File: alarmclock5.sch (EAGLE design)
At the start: 39 parts, among them X1 MKDSN1,5/2-5,08, X2 MKDSN1,5/2-5,08, X3 MKDSN1,5/2-5,08, X4 MKDSN1,5/2-5,08

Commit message: new schema
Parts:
- added C16: 330uF/25V, SparkFun-Passives:CAP_POLPTH2
- added Q1: FDN360P, transistor-power:FDN360P
- added R11: 10k, SparkFun-Passives:RESISTOR0603-RES
- added T1: 2N2222, transistor:2N2222
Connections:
- new net N$40: T1.B, U$5.IO8
- new net N$41: Q1.G, R11.1, T1.C
- new net N$43: Q1.S, R11.2, U$1.VCC, U$2.VIN+
- net GND: now also C16.-, T1.E
- net VCC: now also C16.+, Q1.D; no longer U$1.VCC, U$2.VIN+
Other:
- moved on the sheet: C11, U$1, U$2, U$4
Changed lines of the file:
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@@
 <part name="U$1" library="mouser" deviceset="163-179PH-EX" device=""/>
 <part name="U$2" library="mouser" deviceset="709-SMU02N-05" device=""/>
-<part name="SUPPLY1" library="SparkFun-Aesthetics" deviceset="VCC" device=""/>
 <part name="GND1" library="SparkFun-Aesthetics" deviceset="GND" device=""/>
 <part name="U$4" library="mouser" deviceset="USB_TYPEA_CONNECTOR" device=""/>
@@
 <part name="C15" library="SparkFun-Capacitors" deviceset="CAP" device="0603-CAP" value="2200pF50V"/>
 <part name="SUPPLY30" library="supply2" deviceset="GND" device=""/>
+<part name="T1" library="transistor" deviceset="2N2222" device=""/>
+<part name="GND2" library="SparkFun-Aesthetics" deviceset="GND" device=""/>
+<part name="R11" library="SparkFun-Passives" deviceset="RESISTOR" device="0603-RES" value="10k"/>
+<part name="Q1" library="transistor-power" deviceset="FDN360P" device=""/>
+<part name="GND3" library="SparkFun-Aesthetics" deviceset="GND" device=""/>
+<part name="SUPPLY31" library="SparkFun-Aesthetics" deviceset="VCC" device=""/>
+<part name="C16" library="SparkFun-Passives" deviceset="CAP_POL" device="PTH2" value="330uF/25V"/>
 </parts>
 <sheets>
 <sheet>
 <plain>
-<text x="152.4" y="76.2" size="1.778" layer="91">18V</text>
+<text x="-83.82" y="-132.08" size="1.778" layer="91">18V</text>
 </plain>
 <instances>
-<instance part="U$1" gate="G$1" x="139.7" y="76.2"/>
-<instance part="U$2" gate="G$1" x="96.52" y="73.66"/>
-<instance part="SUPPLY1" gate="G$1" x="127" y="78.74"/>
-<instance part="GND1" gate="1" x="127" y="71.12"/>
-<instance part="U$4" gate="G$1" x="45.72" y="76.2"/>
+<instance part="U$1" gate="G$1" x="-96.52" y="-132.08"/>
+<instance part="U$2" gate="G$1" x="-139.7" y="-134.62"/>
+<instance part="GND1" gate="1" x="-109.22" y="-137.16"/>
+<instance part="U$4" gate="G$1" x="-190.5" y="-132.08"/>
 <instance part="U$3" gate="G$1" x="116.84" y="-17.78"/>
 <instance part="GND4" gate="1" x="157.48" y="-63.5"/>
@@
 <instance part="R3" gate="G$1" x="129.54" y="-78.74" rot="R90"/>
 <instance part="R1" gate="G$1" x="114.3" y="-15.24" rot="R90"/>
-<instance part="C11" gate="G$1" x="73.66" y="76.2"/>
+<instance part="C11" gate="G$1" x="-162.56" y="-132.08"/>
 <instance part="SUPPLY6" gate="GND" x="127" y="-7.62" rot="R180"/>
 <instance part="+3V1" gate="G$1" x="-20.32" y="27.94"/>
@@
 <instance part="C15" gate="G$1" x="101.6" y="-48.26" rot="R90"/>
 <instance part="SUPPLY30" gate="GND" x="106.68" y="-48.26" rot="R90"/>
+<instance part="T1" gate="G$1" x="-50.8" y="-96.52" rot="MR0"/>
+<instance part="GND2" gate="1" x="-53.34" y="-106.68" rot="MR0"/>
+<instance part="R11" gate="G$1" x="-53.34" y="-81.28" rot="MR90"/>
+<instance part="Q1" gate="G$1" x="-66.04" y="-93.98" rot="MR0"/>
+<instance part="GND3" gate="1" x="-78.74" y="-109.22" rot="MR0"/>
+<instance part="SUPPLY31" gate="G$1" x="-78.74" y="-99.06" rot="MR0"/>
+<instance part="C16" gate="G$1" x="-78.74" y="-101.6" rot="MR0"/>
 </instances>
 <busses>
@@
 <segment>
 <pinref part="U$2" gate="G$1" pin="VO+"/>
-<wire x1="63.5" y1="78.74" x2="73.66" y2="78.74" width="0.1524" layer="91"/>
+<wire x1="-172.72" y1="-129.54" x2="-162.56" y2="-129.54" width="0.1524" layer="91"/>
 <pinref part="U$4" gate="G$1" pin="VCC"/>
-<wire x1="73.66" y1="78.74" x2="86.36" y2="78.74" width="0.1524" layer="91"/>
-<wire x1="35.56" y1="83.82" x2="35.56" y2="91.44" width="0.1524" layer="91"/>
-<wire x1="35.56" y1="91.44" x2="63.5" y2="91.44" width="0.1524" layer="91"/>
-<wire x1="63.5" y1="91.44" x2="63.5" y2="78.74" width="0.1524" layer="91"/>
+<wire x1="-162.56" y1="-129.54" x2="-149.86" y2="-129.54" width="0.1524" layer="91"/>
+<wire x1="-200.66" y1="-124.46" x2="-200.66" y2="-116.84" width="0.1524" layer="91"/>
+<wire x1="-200.66" y1="-116.84" x2="-172.72" y2="-116.84" width="0.1524" layer="91"/>
+<wire x1="-172.72" y1="-116.84" x2="-172.72" y2="-129.54" width="0.1524" layer="91"/>
 <pinref part="C11" gate="G$1" pin="+"/>
-<junction x="73.66" y="78.74"/>
+<junction x="-162.56" y="-129.54"/>
 </segment>
 </net>
 <net name="VCC" class="1">
-<segment>
-<pinref part="U$2" gate="G$1" pin="VIN+"/>
-<pinref part="U$1" gate="G$1" pin="VCC"/>
-<wire x1="111.76" y1="78.74" x2="127" y2="78.74" width="0.1524" layer="91"/>
-<pinref part="SUPPLY1" gate="G$1" pin="VCC"/>
-<wire x1="127" y1="78.74" x2="134.62" y2="78.74" width="0.1524" layer="91"/>
-<junction x="127" y="78.74"/>
-</segment>
 <segment>
 <pinref part="SUPPLY5" gate="G$1" pin="VCC"/>
@@
 <junction x="157.48" y="-50.8"/>
 </segment>
+<segment>
+<pinref part="SUPPLY31" gate="G$1" pin="VCC"/>
+<pinref part="C16" gate="G$1" pin="+"/>
+<pinref part="Q1" gate="G$1" pin="D"/>
+<wire x1="-68.58" y1="-99.06" x2="-78.74" y2="-99.06" width="0.1524" layer="91"/>
+</segment>
 </net>
 <net name="GND" class="1">
@@
 <pinref part="U$1" gate="G$1" pin="GND"/>
 <pinref part="U$2" gate="G$1" pin="VIN-"/>
-<wire x1="134.62" y1="73.66" x2="127" y2="73.66" width="0.1524" layer="91"/>
+<wire x1="-101.6" y1="-134.62" x2="-109.22" y2="-134.62" width="0.1524" layer="91"/>
 <pinref part="GND1" gate="1" pin="GND"/>
-<wire x1="127" y1="73.66" x2="111.76" y2="73.66" width="0.1524" layer="91"/>
-<junction x="127" y="73.66"/>
-<wire x1="134.62" y1="73.66" x2="134.62" y2="68.58" width="0.1524" layer="91"/>
-<wire x1="134.62" y1="68.58" x2="154.94" y2="68.58" width="0.1524" layer="91"/>
+<wire x1="-109.22" y1="-134.62" x2="-124.46" y2="-134.62" width="0.1524" layer="91"/>
+<junction x="-109.22" y="-134.62"/>
+<wire x1="-101.6" y1="-134.62" x2="-101.6" y2="-139.7" width="0.1524" layer="91"/>
+<wire x1="-101.6" y1="-139.7" x2="-81.28" y2="-139.7" width="0.1524" layer="91"/>
 <pinref part="U$1" gate="G$1" pin="GND1"/>
-<wire x1="154.94" y1="68.58" x2="154.94" y2="76.2" width="0.1524" layer="91"/>
-<junction x="134.62" y="73.66"/>
+<wire x1="-81.28" y1="-139.7" x2="-81.28" y2="-132.08" width="0.1524" layer="91"/>
+<junction x="-101.6" y="-134.62"/>
 </segment>
 <segment>
@@
 <pinref part="C15" gate="G$1" pin="2"/>
 <pinref part="SUPPLY30" gate="GND" pin="GND"/>
+</segment>
+<segment>
+<pinref part="T1" gate="G$1" pin="E"/>
+<pinref part="GND2" gate="1" pin="GND"/>
+<wire x1="-53.34" y1="-104.14" x2="-53.34" y2="-101.6" width="0.1524" layer="91"/>
+</segment>
+<segment>
+<pinref part="C16" gate="G$1" pin="-"/>
+<pinref part="GND3" gate="1" pin="GND"/>
 </segment>
 </net>
@@
 <segment>
 <pinref part="U$2" gate="G$1" pin="VO-"/>
-<wire x1="86.36" y1="73.66" x2="76.2" y2="73.66" width="0.1524" layer="91"/>
-<wire x1="76.2" y1="73.66" x2="73.66" y2="71.12" width="0.1524" layer="91"/>
-<wire x1="73.66" y1="71.12" x2="63.5" y2="71.12" width="0.1524" layer="91"/>
+<wire x1="-149.86" y1="-134.62" x2="-160.02" y2="-134.62" width="0.1524" layer="91"/>
+<wire x1="-160.02" y1="-134.62" x2="-162.56" y2="-137.16" width="0.1524" layer="91"/>
+<wire x1="-162.56" y1="-137.16" x2="-172.72" y2="-137.16" width="0.1524" layer="91"/>
 <pinref part="U$4" gate="G$1" pin="GND"/>
-<wire x1="35.56" y1="68.58" x2="35.56" y2="58.42" width="0.1524" layer="91"/>
-<wire x1="35.56" y1="58.42" x2="63.5" y2="58.42" width="0.1524" layer="91"/>
-<wire x1="63.5" y1="58.42" x2="63.5" y2="71.12" width="0.1524" layer="91"/>
+<wire x1="-200.66" y1="-139.7" x2="-200.66" y2="-149.86" width="0.1524" layer="91"/>
+<wire x1="-200.66" y1="-149.86" x2="-172.72" y2="-149.86" width="0.1524" layer="91"/>
+<wire x1="-172.72" y1="-149.86" x2="-172.72" y2="-137.16" width="0.1524" layer="91"/>
 <pinref part="C11" gate="G$1" pin="-"/>
-<junction x="73.66" y="71.12"/>
+<junction x="-162.56" y="-137.16"/>
 </segment>
 </net>
@@
 </segment>
 </net>
+<net name="N$40" class="0">
+<segment>
+<pinref part="U$5" gate="G$1" pin="IO8"/>
+<wire x1="-20.32" y1="-63.5" x2="-48.26" y2="-63.5" width="0.1524" layer="91"/>
+<pinref part="T1" gate="G$1" pin="B"/>
+<wire x1="-48.26" y1="-63.5" x2="-48.26" y2="-96.52" width="0.1524" layer="91"/>
+</segment>
+</net>
+<net name="N$41" class="0">
+<segment>
+<pinref part="T1" gate="G$1" pin="C"/>
+<pinref part="R11" gate="G$1" pin="1"/>
+<wire x1="-53.34" y1="-86.36" x2="-53.34" y2="-91.44" width="0.1524" layer="91"/>
+<pinref part="Q1" gate="G$1" pin="G"/>
+<wire x1="-63.5" y1="-91.44" x2="-53.34" y2="-91.44" width="0.1524" layer="91"/>
+</segment>
+</net>
+<net name="N$43" class="0">
+<segment>
+<pinref part="U$1" gate="G$1" pin="VCC"/>
+<pinref part="U$2" gate="G$1" pin="VIN+"/>
+<wire x1="-101.6" y1="-129.54" x2="-124.46" y2="-129.54" width="0.1524" layer="91"/>
+<wire x1="-101.6" y1="-129.54" x2="-101.6" y2="-76.2" width="0.1524" layer="91"/>
+<pinref part="Q1" gate="G$1" pin="S"/>
+<wire x1="-68.58" y1="-88.9" x2="-68.58" y2="-76.2" width="0.1524" layer="91"/>
+<pinref part="R11" gate="G$1" pin="2"/>
+<wire x1="-68.58" y1="-76.2" x2="-53.34" y2="-76.2" width="0.1524" layer="91"/>
+<wire x1="-101.6" y1="-76.2" x2="-53.34" y2="-76.2" width="0.1524" layer="91"/>
+<junction x="-53.34" y="-76.2"/>
+<junction x="-101.6" y="-129.54"/>
+</segment>
+</net>

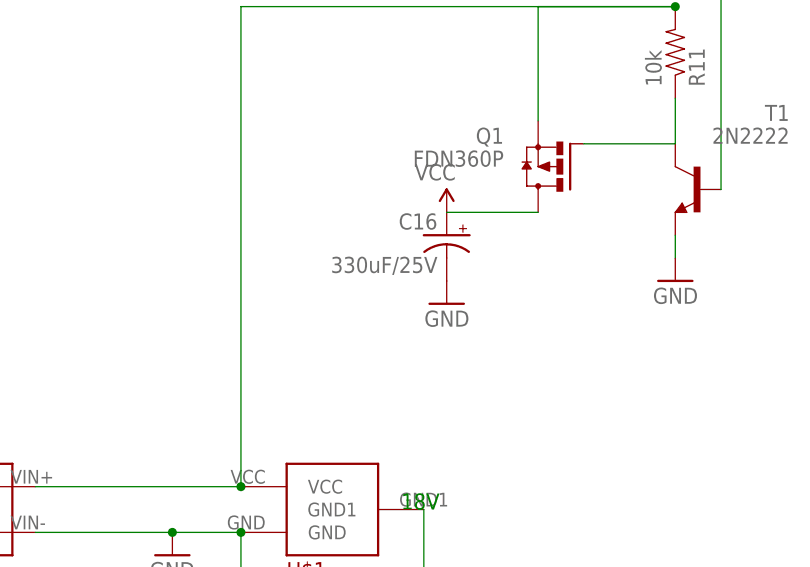
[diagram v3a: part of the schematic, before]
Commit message: add a R10k resistor to flush the capa
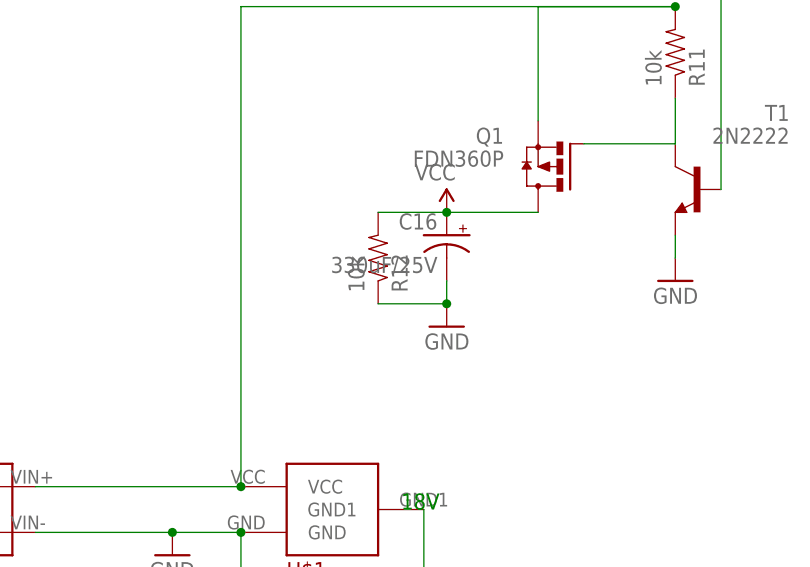
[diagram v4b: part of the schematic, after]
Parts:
- added R12: 10k, SparkFun-Passives:RESISTOR0603-RES
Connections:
- net GND: now also R12.1
- net VCC: now also R12.2
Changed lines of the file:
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@@
 <part name="SUPPLY31" library="SparkFun-Aesthetics" deviceset="VCC" device=""/>
 <part name="C16" library="SparkFun-Passives" deviceset="CAP_POL" device="PTH2" value="330uF/25V"/>
+<part name="R12" library="SparkFun-Passives" deviceset="RESISTOR" device="0603-RES" value="10k"/>
 </parts>
 <sheets>
@@
 <instance part="R11" gate="G$1" x="-53.34" y="-81.28" rot="MR90"/>
 <instance part="Q1" gate="G$1" x="-66.04" y="-93.98" rot="MR0"/>
-<instance part="GND3" gate="1" x="-78.74" y="-109.22" rot="MR0"/>
+<instance part="GND3" gate="1" x="-78.74" y="-111.76" rot="MR0"/>
 <instance part="SUPPLY31" gate="G$1" x="-78.74" y="-99.06" rot="MR0"/>
 <instance part="C16" gate="G$1" x="-78.74" y="-101.6" rot="MR0"/>
+<instance part="R12" gate="G$1" x="-86.36" y="-104.14" rot="MR90"/>
 </instances>
 <busses>
@@
 <pinref part="Q1" gate="G$1" pin="D"/>
 <wire x1="-68.58" y1="-99.06" x2="-78.74" y2="-99.06" width="0.1524" layer="91"/>
+<pinref part="R12" gate="G$1" pin="2"/>
+<wire x1="-78.74" y1="-99.06" x2="-86.36" y2="-99.06" width="0.1524" layer="91"/>
+<junction x="-78.74" y="-99.06"/>
 </segment>
 </net>
@@
 <pinref part="C16" gate="G$1" pin="-"/>
 <pinref part="GND3" gate="1" pin="GND"/>
+<wire x1="-78.74" y1="-109.22" x2="-78.74" y2="-106.68" width="0.1524" layer="91"/>
+<pinref part="R12" gate="G$1" pin="1"/>
+<wire x1="-78.74" y1="-109.22" x2="-86.36" y2="-109.22" width="0.1524" layer="91"/>
+<junction x="-78.74" y="-109.22"/>
 </segment>
 </net>

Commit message: update especially mouser.lbr
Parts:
- C16: value 330uF/25V -> 680uF/25V
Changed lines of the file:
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@@
 <part name="GND3" library="SparkFun-Aesthetics" deviceset="GND" device=""/>
 <part name="SUPPLY31" library="SparkFun-Aesthetics" deviceset="VCC" device=""/>
-<part name="C16" library="SparkFun-Passives" deviceset="CAP_POL" device="PTH2" value="330uF/25V"/>
+<part name="C16" library="SparkFun-Passives" deviceset="CAP_POL" device="PTH2" value="680uF/25V"/>
 <part name="R12" library="SparkFun-Passives" deviceset="RESISTOR" device="0603-RES" value="10k"/>
 </parts>
